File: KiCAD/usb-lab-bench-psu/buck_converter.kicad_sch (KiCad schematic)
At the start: 32 parts, among them J3 Conn_02x03_Top_Bottom, J4 Conn_02x01, U10 LM73100, U5 AP63203WU, U9 LM73100

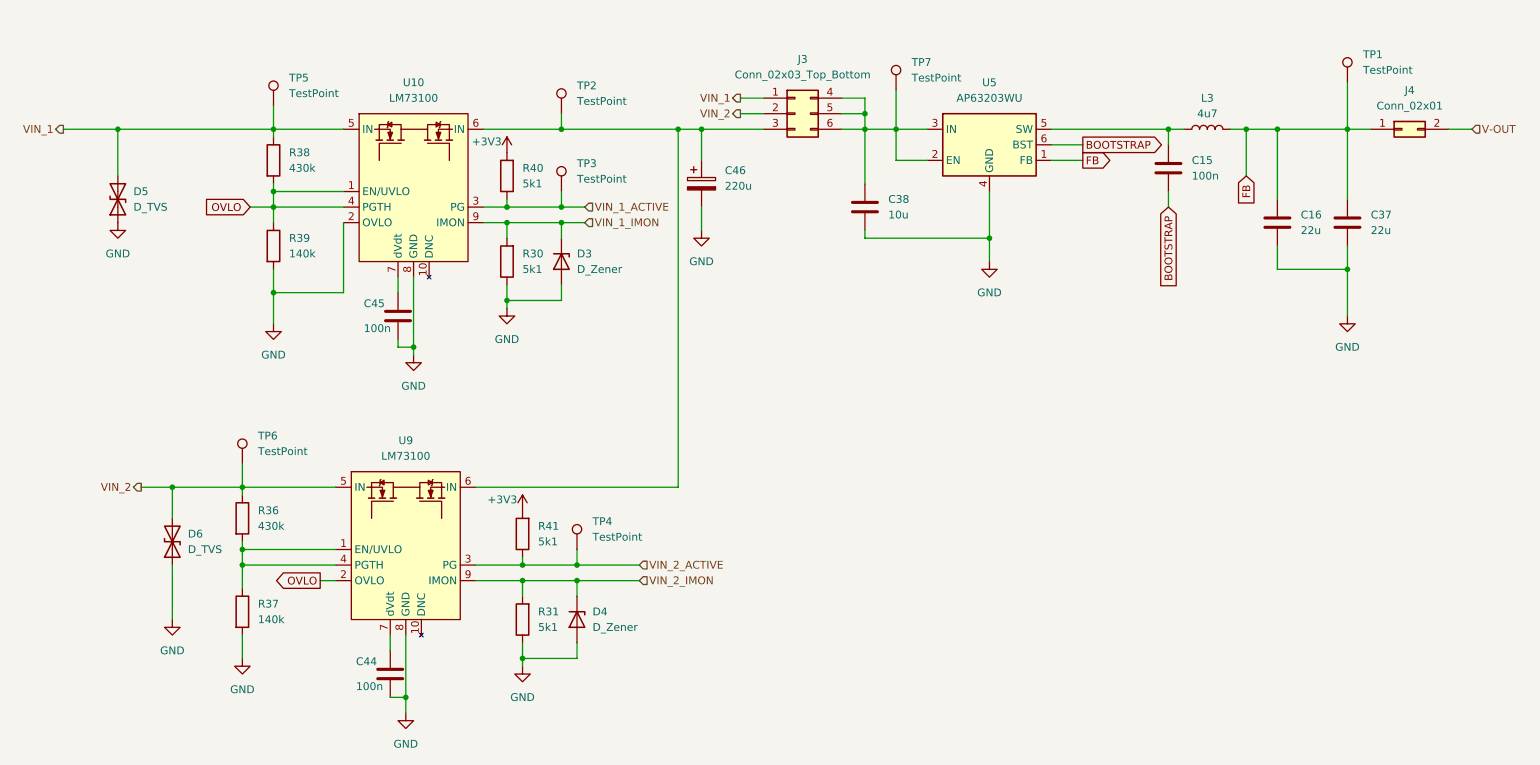
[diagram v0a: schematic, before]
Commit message: Replaced global labels with labels, added measurement circuit, started with io board
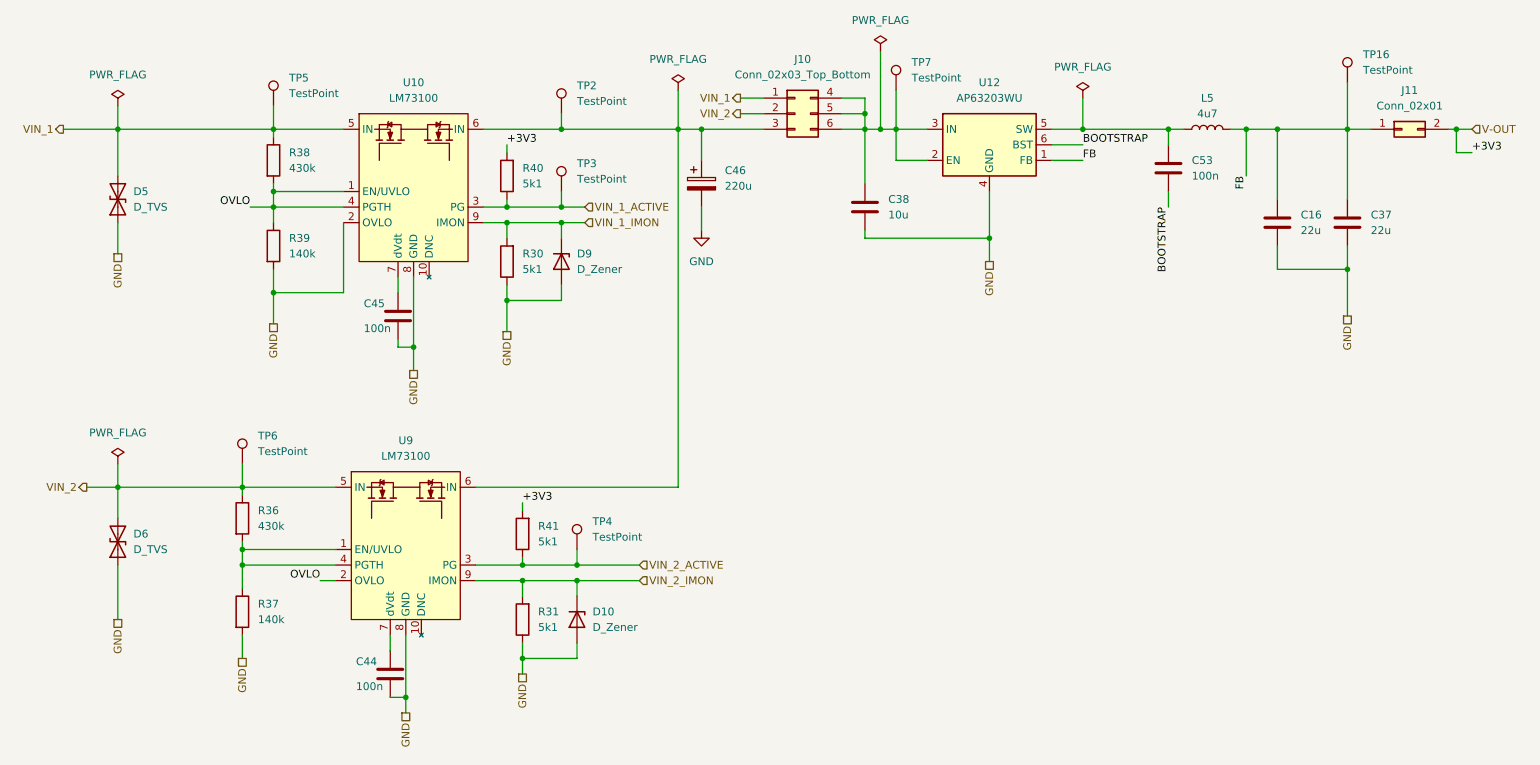
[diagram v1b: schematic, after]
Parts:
- renumbered C15 to C53, D4 to D10, D3 to D9, J3 to J10, J4 to J11, L3 to L5, TP1 to TP16, U5 to U12
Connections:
- net +3V3 is gone; now on net V-OUT: R40.2, R41.2
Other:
- moved on the sheet: D6

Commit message: updated GND and supply nets, switched buck-boost-converter
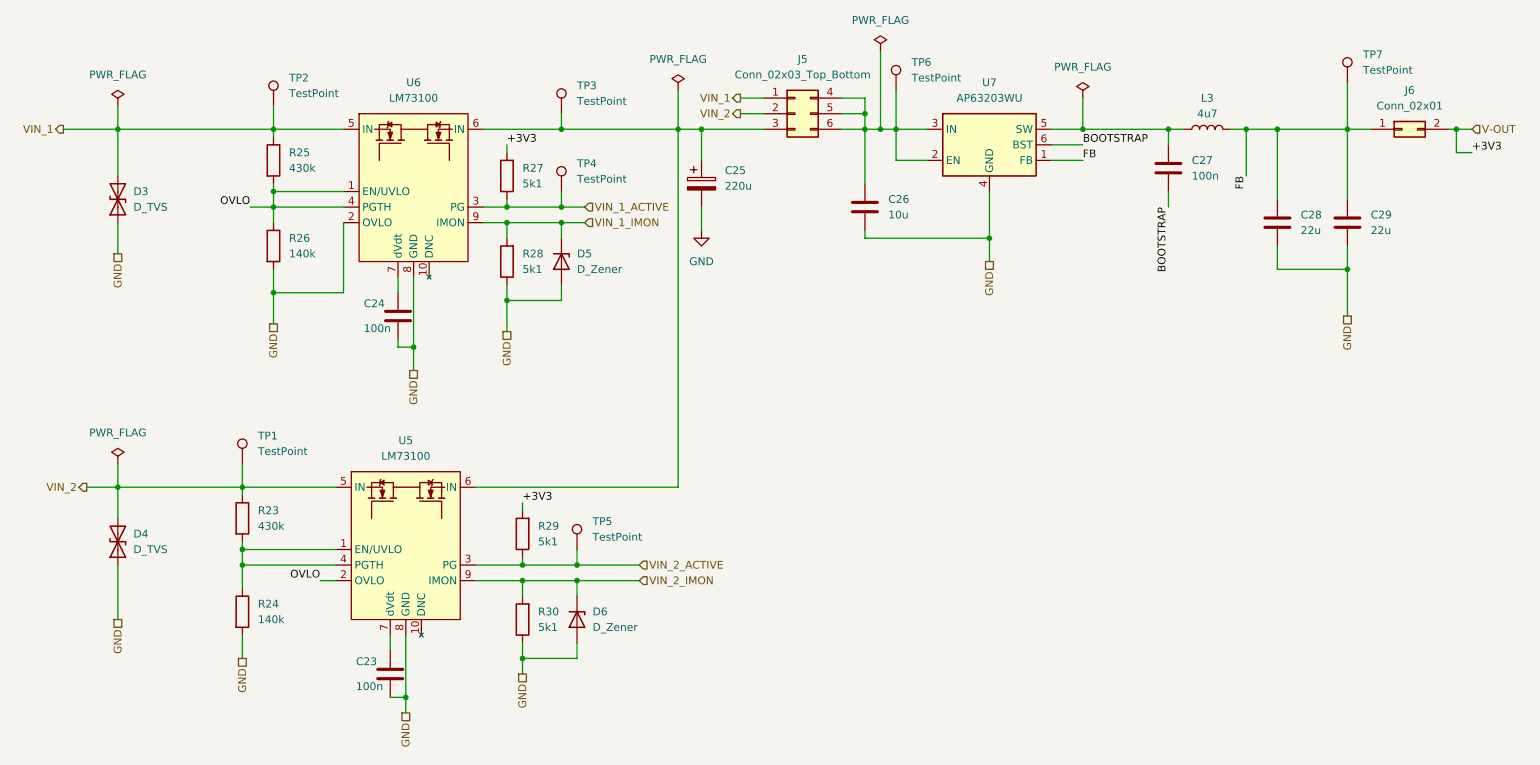
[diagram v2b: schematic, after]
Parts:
- renumbered C44 to C23, C45 to C24, C46 to C25, C38 to C26, C53 to C27, C16 to C28, C37 to C29, D5 to D3, D6 to D4, D9 to D5, D10 to D6, J10 to J5, J11 to J6, L5 to L3, R36 to R23, R37 to R24, R38 to R25, R39 to R26, R40 to R27, R30 to R28, R41 to R29, R31 to R30, TP6 to TP1, TP5 to TP2, TP2 to TP3, TP3 to TP4, TP4 to TP5, TP7 to TP6, TP16 to TP7, U9 to U5, U10 to U6, U12 to U7

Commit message: adapted buck converter
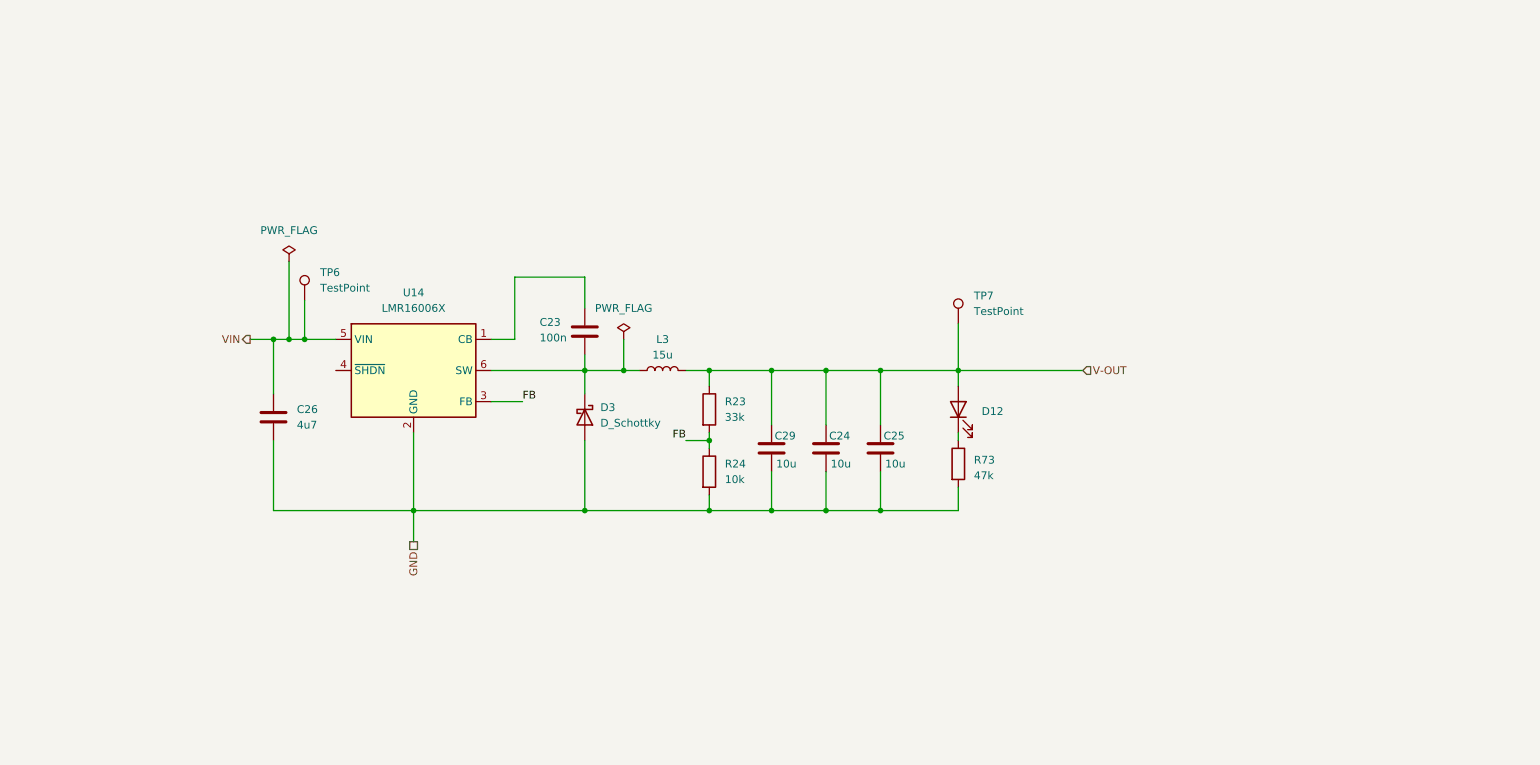
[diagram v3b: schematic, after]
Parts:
- removed C25: 220u, symbol Device:C_Polarized
- removed C27: 100n, symbol Device:C
- removed C28: 22u, symbol Device:C
- removed D3, D4: D_TVS, symbol Device:D_TVS
- removed D5, D6: D_Zener, symbol Device:D_Zener
- removed J5: Conn_02x03_Top_Bottom, symbol Connector_Generic:Conn_02x03_Top_Bottom
- removed J6: Conn_02x01, symbol Connector_Generic:Conn_02x01
- removed R25: 430k, symbol Device:R
- removed R26: 140k, symbol Device:R
- removed R27, R28, R29, R30: 5k1, symbol Device:R
- removed TP1, TP2, TP3, TP4, TP5: TestPoint, symbol Connector:TestPoint
- removed U5, U6: LM73100, Prj_QFN:RPW0010A-MFG, symbol Prj_power:LM73100
- removed U7: AP63203WU, Package_TO_SOT_SMD:TSOT-23-6, symbol Regulator_Switching:AP63203WU
- added C25: 10u, symbol Device:C
- added D12: XL-1005UGC, Diode_SMD:D_0402_1005Metric_Pad0.77x0.64mm_HandSolder, symbol Device:LED
- added D3: D_Schottky, symbol Device:D_Schottky
- added R73: 47k, Resistor_SMD:R_0402_1005Metric_Pad0.72x0.64mm_HandSolder, symbol Device:R
- added U14: LMR16006X, Package_TO_SOT_SMD:TSOT-23-6, symbol Prj_dcdc_converter:LMR16006X
- C24: value 100n -> 10u
- C26: value 10u -> 4u7
- C29: value 22u -> 10u
- L3: value 4u7 -> 15u
- R23: value 430k -> 33k; footprint (none) -> Resistor_SMD:R_0402_1005Metric_Pad0.72x0.64mm_HandSolder
- R24: value 140k -> 10k; footprint (none) -> Resistor_SMD:R_0402_1005Metric_Pad0.72x0.64mm_HandSolder
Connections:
- net VIN_2 is gone; now on net V-OUT: R23.1
- net FB: now also R23.2, R24.1, U14.3 (FB); no longer C29.1, L3.2, TP7.1
- net GND: now also C24.2, C25.2, D3.2 (A), R73.2, U14.2 (GND); no longer C23.1, C24.1
- net V-OUT: now also C24.1, C29.1, L3.2, TP7.1, C25.1, D12.2 (A)
- net VIN: now reaches C26.1, TP6.1
- net VIN: now also U14.5 (VIN)
- net at L3.1: now also C23.2, D3.1 (K), U14.6 (SW)
- new net: D12.1 (K), R73.1
- new net: C23.1, U14.1 (CB)
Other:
- moved on the sheet: C26, C29, L3, TP6, TP7
